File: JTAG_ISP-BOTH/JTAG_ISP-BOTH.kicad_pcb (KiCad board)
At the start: 2 copper layers, 48.9 x 46.1 mm, 21 parts, among them J1 Conn_01x08, J1 Conn_02x03_Odd_Even, J2 Conn_01x08, J3 Conn_01x08

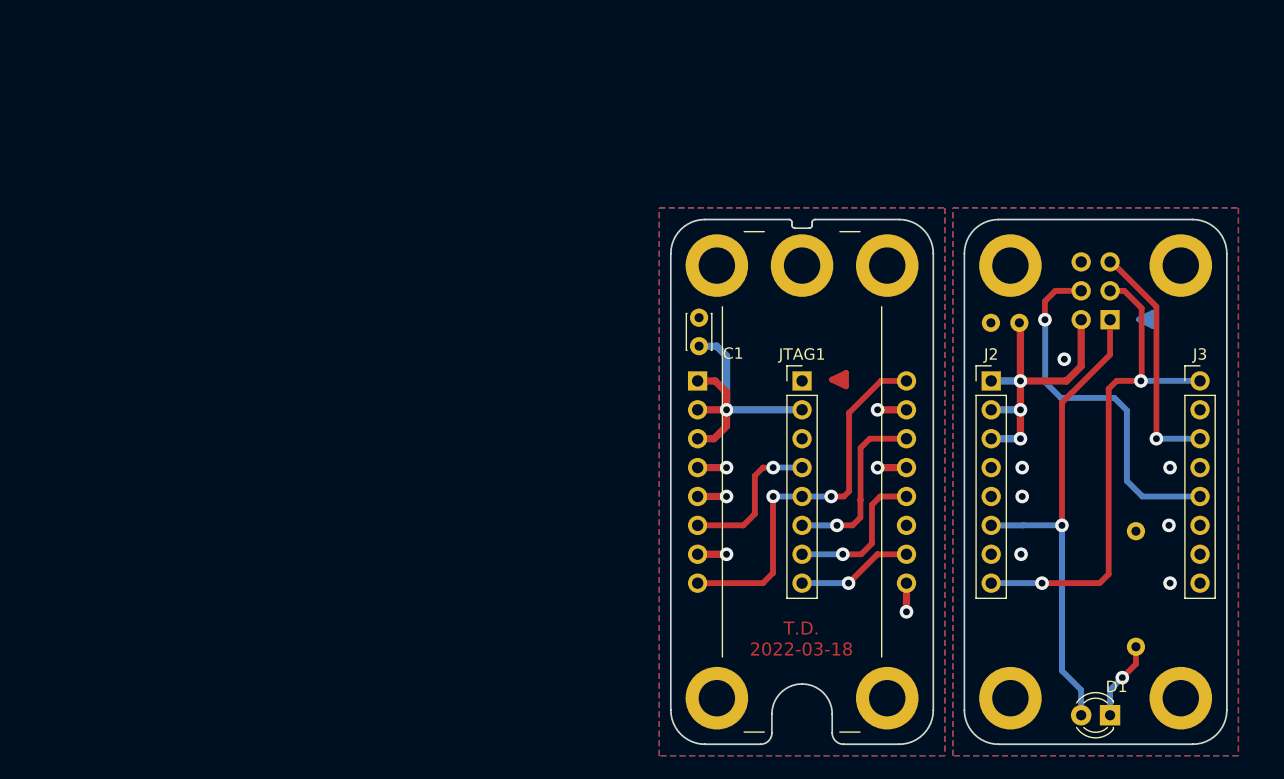
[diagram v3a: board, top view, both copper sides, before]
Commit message: # [PCB] + Création d'une archive PROD_LPKF.zip qui contient les fichiers envoyés pour fabrication. * Nouveau format de page A5. * Mise à jour des fichiers gerbers du projet BOTH. * Mise à jour de la cartouche pour le projet BOTH.     * Date actuelle;     * Version actuelle.
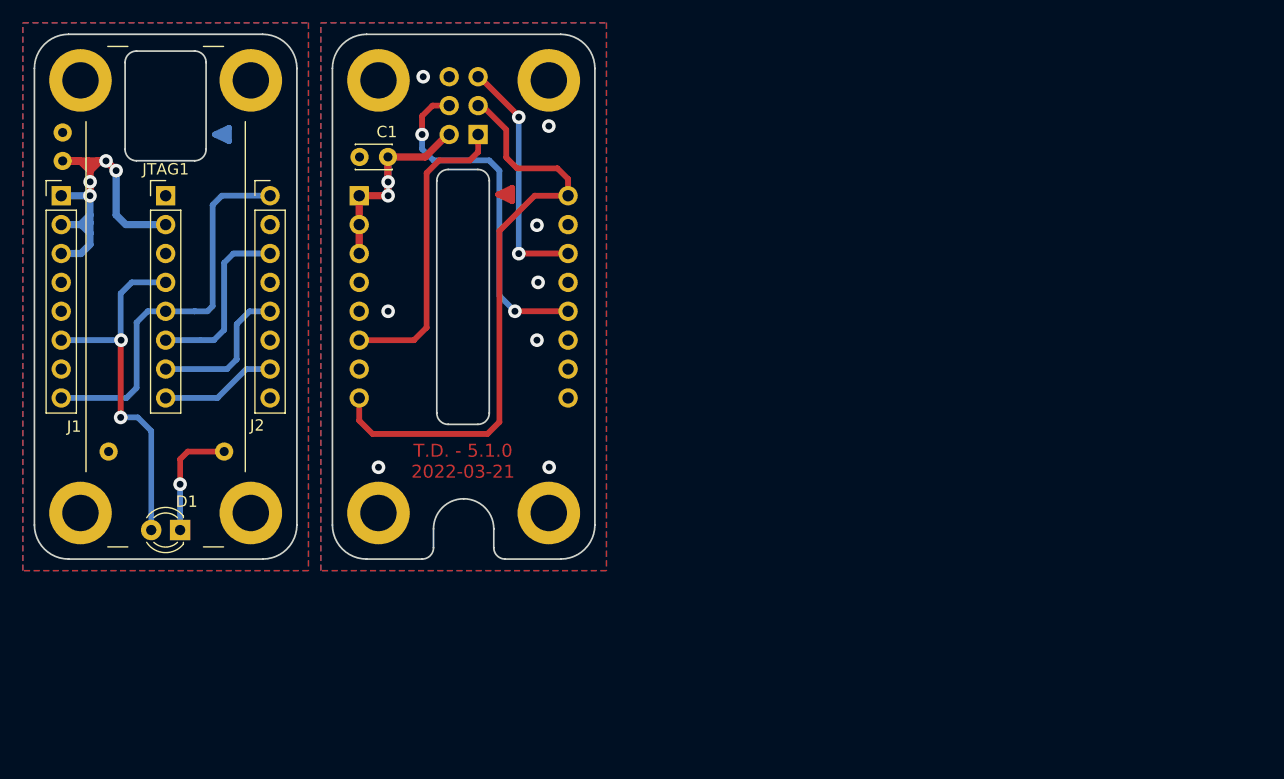
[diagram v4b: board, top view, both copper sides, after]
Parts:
- removed the C1 at (147.3, 72.5)
- removed the C1 at (175.4, 70.5)
- removed the J1 at (183.4, 70.2)
- removed the J1 at (147.1, 75.6)
- removed the J2 at (172.9, 75.6)
- removed the J2 at (165.5, 75.6)
- removed the REF** at (189.6, 65.5)
- removed the REF** at (163.8, 103.5)
- removed the REF** at (187.2, 70.5)
- removed the REF** at (148.8, 65.5)
- removed the REF** at (148.8, 103.5)
- removed the REF** at (189.6, 103.5)
- removed the REF** at (156.3, 65.5)
- removed the REF** at (174.6, 103.5)
- removed the REF** at (160.2, 75.1)
- removed the REF** at (174.6, 65.5)
- removed the REF** at (163.8, 65.5)
- added C1: 100nF, Capacitor_THT:C_Disc_D3.0mm_W2.0mm_P2.50mm, F.Cu at (119.9, 55.9)
- added C1: 100nF, Capacitor_THT:C_Disc_D3.0mm_W2.0mm_P2.50mm, B.Cu at (91.3, 56.3)
- added J1: Conn_01x08, Connector_PinHeader_2.54mm:PinHeader_1x08_P2.54mm_Vertical, F.Cu at (91.2, 59.3)
- added J1: Conn_02x03_Odd_Even, Connector_PinSocket_2.54mm:PinSocket_2x03_P2.54mm_Vertical, B.Cu at (127.8, 53.9)
- added J2: Conn_01x08, Connector_PinHeader_2.54mm:PinHeader_1x08_P2.54mm_Vertical, F.Cu at (109.5, 59.3)
- added J2: Conn_01x08, Connector_PinHeader_2.54mm:PinHeader_1x08_P2.54mm_Vertical, B.Cu at (117.4, 59.3)
- added REF**: MountingHole_3.2mm_M3_ISO14580_Pad, MountingHole:MountingHole_3.2mm_M3_ISO14580_Pad, F.Cu at (92.9, 49.2)
- added REF**: Fleche_small, THOMAS_library:Fleche_small, B.Cu at (105.9, 54.3)
- added REF**: Fleche_small, THOMAS_library:Fleche_small, F.Cu at (130.8, 58.9)
- added REF**: MountingHole_3.2mm_M3_ISO14580_Pad, MountingHole:MountingHole_3.2mm_M3_ISO14580_Pad, F.Cu at (134.0, 87.2)
- added REF**: MountingHole_3.2mm_M3_ISO14580_Pad, MountingHole:MountingHole_3.2mm_M3_ISO14580_Pad, F.Cu at (92.9, 87.2)
- added REF**: MountingHole_3.2mm_M3_ISO14580_Pad, MountingHole:MountingHole_3.2mm_M3_ISO14580_Pad, F.Cu at (107.8, 87.2)
- added REF**: MountingHole_3.2mm_M3_ISO14580_Pad, MountingHole:MountingHole_3.2mm_M3_ISO14580_Pad, F.Cu at (119.1, 49.2)
- added REF**: MountingHole_3.2mm_M3_ISO14580_Pad, MountingHole:MountingHole_3.2mm_M3_ISO14580_Pad, F.Cu at (107.8, 49.2)
- added REF**: MountingHole_3.2mm_M3_ISO14580_Pad, MountingHole:MountingHole_3.2mm_M3_ISO14580_Pad, F.Cu at (134.0, 49.2)
- added REF**: MountingHole_3.2mm_M3_ISO14580_Pad, MountingHole:MountingHole_3.2mm_M3_ISO14580_Pad, F.Cu at (119.1, 87.2)
- J3: moved to B.Cu
- R1: value 2k -> 100
- moved D1 83.4 mm to (101.6, 88.7)
- moved R1 82.0 mm to (105.5, 81.8), turned to 180 degrees
- moved JTAG1 58.3 mm to (100.4, 59.3)
- moved J3 57.9 mm to (135.7, 59.3), turned to 180 degrees
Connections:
- D1 pad 2: MISO -> (no net)
- JTAG1 pad 6: (no net) -> RESET
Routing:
- net MISO: track 43.5 -> 26.8 mm, vias 1 -> 0
- net RESET: track 21.1 -> 37.2 mm, vias 1 -> 2
- net GND: track 15.2 -> 0.06 mm, vias 13 -> 8
- net SCLK: track 45.1 -> 52.8 mm, vias 2 -> 0
- net +5V: track 53.7 -> 58.7 mm, vias 4 -> 6
- net (no net): track 85.9 -> 90.1 mm, vias 6 -> 2
- net Net-(D1-Pad1): track 6.96 -> 10.4 mm
- net MOSI: track 32.1 -> 30.9 mm, vias 1 -> 2
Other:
- board size 48.9 x 46.1 mm -> 49.3 x 46.1 mm
- board text added: "T.D. - 5.1.0 2022-03-21"
- board text removed: "T.D. 2022-03-18"

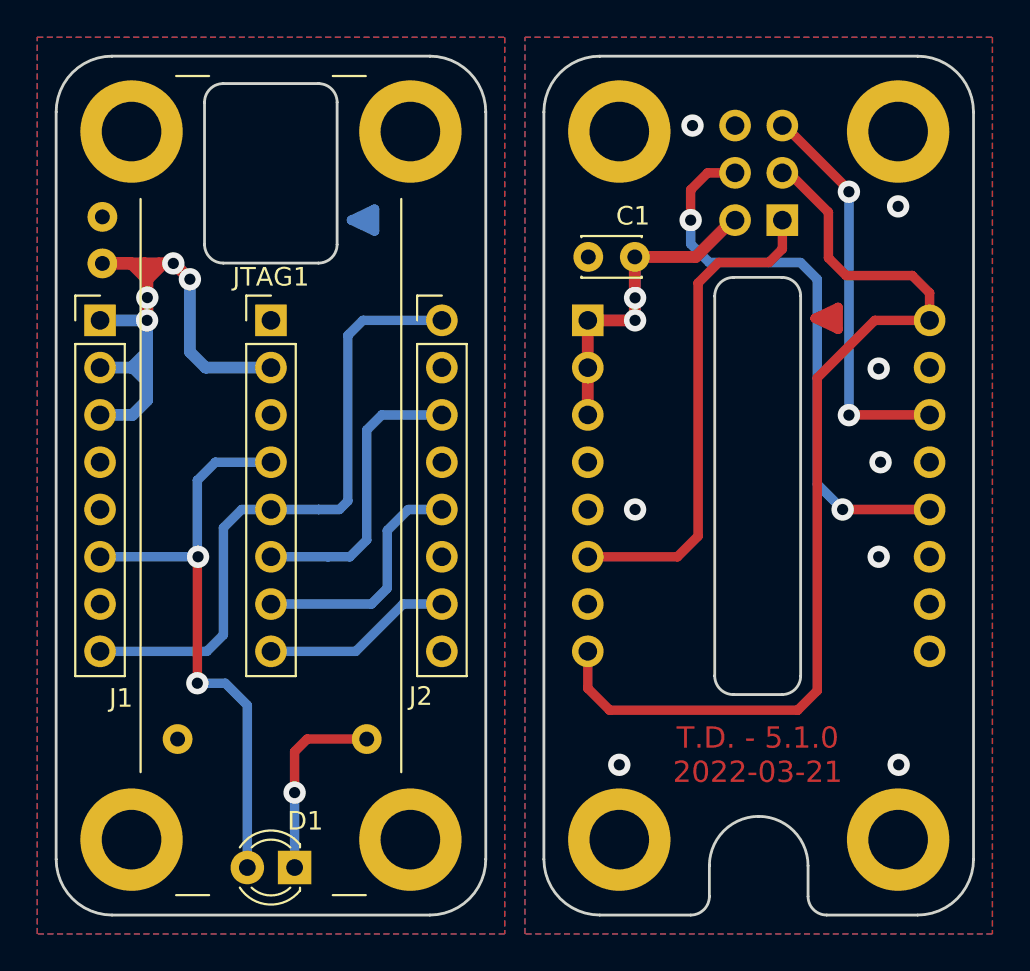
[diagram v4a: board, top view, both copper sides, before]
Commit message: # [PCB] + Création d'une archive PROD_LPKF.zip qui contient les fichiers envoyés pour fabrication. * Mise à jour des fichiers gerbers du projet BOTH. * Mise à jour de la cartouche pour le projet BOTH.     * Date actuelle;     * Version actuelle.
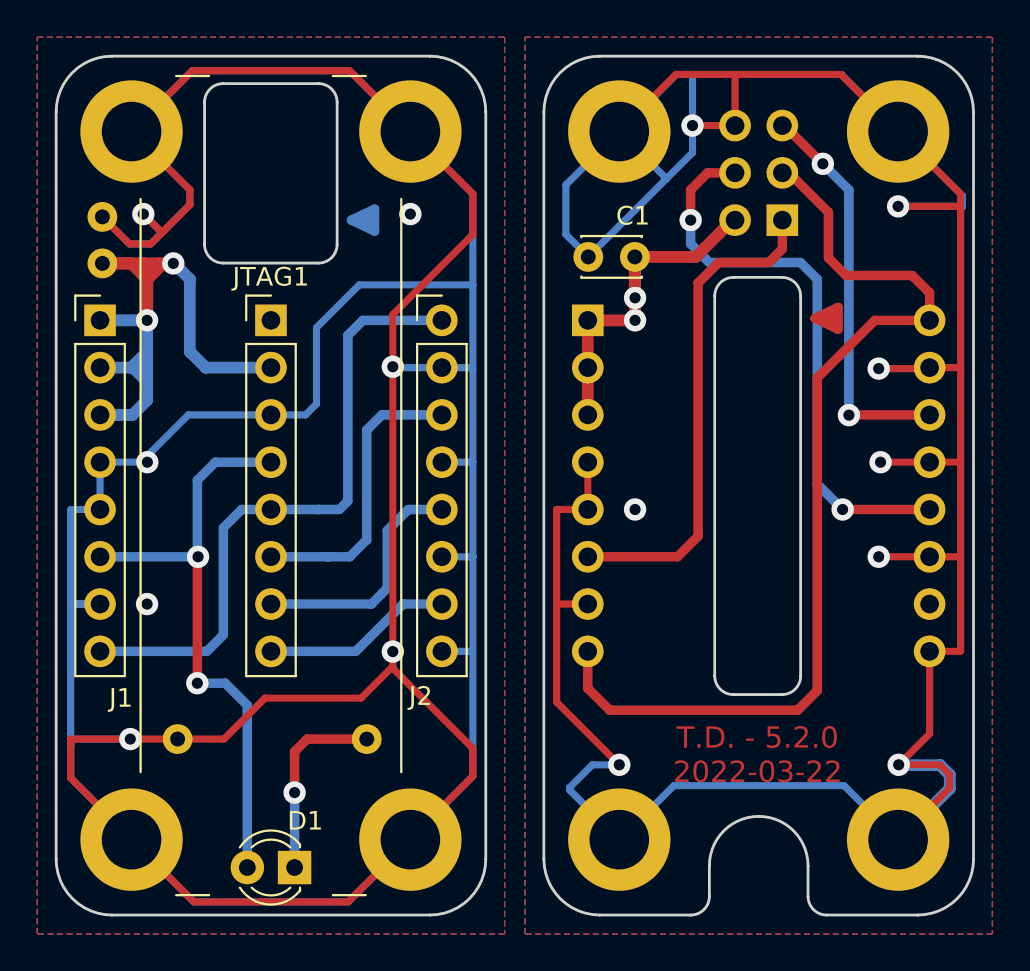
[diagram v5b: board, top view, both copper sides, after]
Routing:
- net GND: track 0.06 -> 461.4 mm, vias 8 -> 15
- net +5V: track 58.7 -> 56.2 mm, vias 6 -> 4
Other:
- board text added: "T.D. - 5.2.0 2022-03-22"
- board text removed: "T.D. - 5.1.0 2022-03-21"

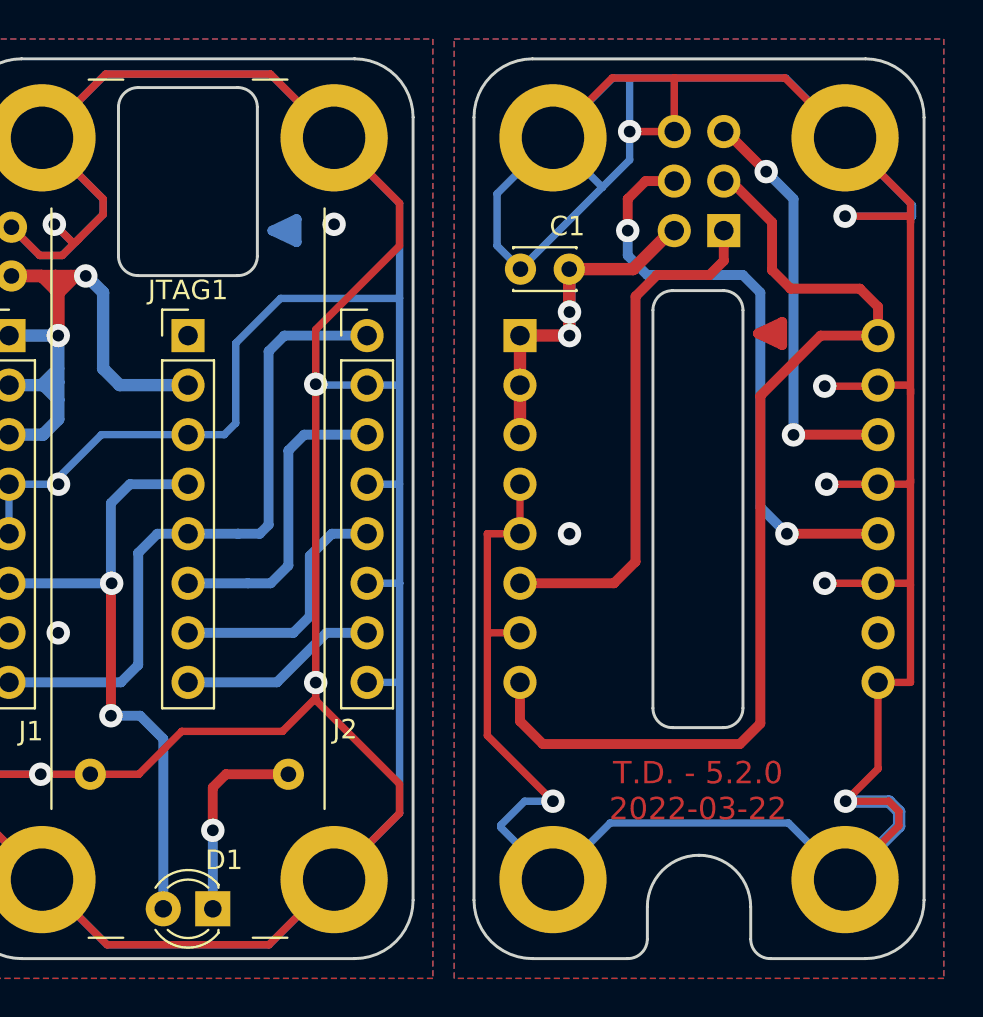
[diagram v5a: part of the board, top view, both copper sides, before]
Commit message: # [PCB] + Création d'une archive PROD_LPKF.zip qui contient les fichiers envoyés pour fabrication. + Ajout de lignes de cote pour le largeur et la hauteur. * Mise à jour des fichiers gerbers du projet BOTH. * Mise à jour de la cartouche pour le projet BOTH.     * Date actuelle;     * Version actuelle.
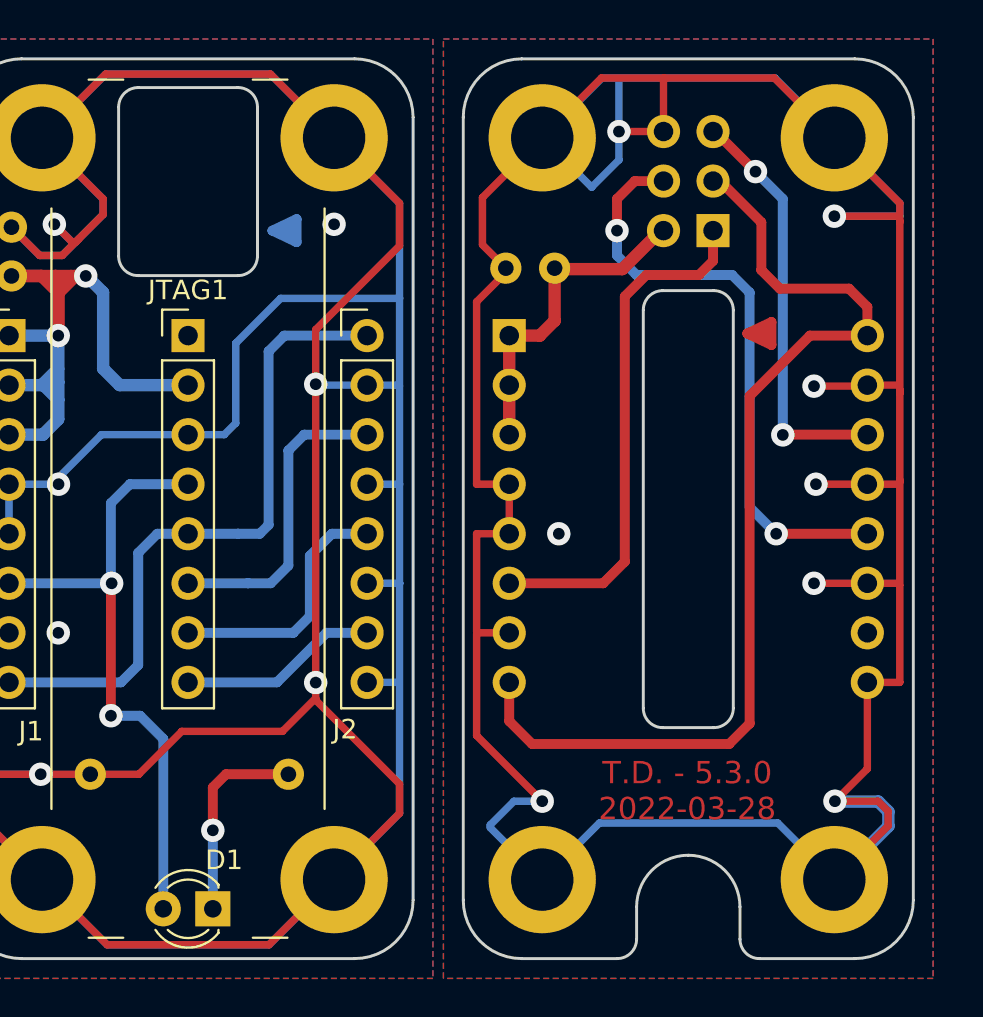
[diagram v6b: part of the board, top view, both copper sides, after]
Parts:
- removed the REF** at (119.1, 49.2)
- removed the REF** at (119.1, 87.2)
- removed the REF** at (134.0, 87.2)
- removed the REF** at (134.0, 49.2)
- added REF**: MountingHole_3.2mm_M3_ISO14580_Pad, MountingHole:MountingHole_3.2mm_M3_ISO14580_Pad, F.Cu at (118.5, 87.2)
- added REF**: MountingHole_3.2mm_M3_ISO14580_Pad, MountingHole:MountingHole_3.2mm_M3_ISO14580_Pad, F.Cu at (118.5, 49.2)
- added REF**: MountingHole_3.2mm_M3_ISO14580_Pad, MountingHole:MountingHole_3.2mm_M3_ISO14580_Pad, F.Cu at (133.5, 87.2)
- added REF**: MountingHole_3.2mm_M3_ISO14580_Pad, MountingHole:MountingHole_3.2mm_M3_ISO14580_Pad, F.Cu at (133.5, 49.2)
- C1: moved to B.Cu
- moved C1 0.75 mm to (119.2, 55.9)
- moved J1 0.55 mm to (127.3, 53.9)
- moved J2 0.55 mm to (116.8, 59.3)
- moved J3 0.55 mm to (135.2, 59.3)
- moved REF** 0.55 mm to (130.3, 58.9)
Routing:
- net GND: track 461.4 -> 468.5 mm
- net +5V: track 56.2 -> 52.0 mm, vias 4 -> 2
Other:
- board size 49.3 x 46.1 mm -> 48.7 x 46.1 mm
- board text added: "T.D. - 5.3.0 2022-03-28"
- board text removed: "T.D. - 5.2.0 2022-03-22"
